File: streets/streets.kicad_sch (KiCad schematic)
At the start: 11 parts, among them J1 Barrel_Jack, J2 Conn_02x20_Odd_Even, J3 Conn_02x20_Odd_Even, J4 Conn_02x20_Odd_Even, J5 Conn_02x20_Odd_Even

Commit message: feat: refactor to use bus
Signed-off-by: Matt Gleich <git@mattglei.ch>
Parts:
- removed S2: M2012SA1W03, M2012SA1W03, symbol M2012SA1W03:M2012SA1W03
- J2: value Conn_02x20_Odd_Even -> Raspberry Pi Zero W 2 (mg01)
- J3: value Conn_02x20_Odd_Even -> Adafruit eINK Bonnet
- J4: value Conn_02x20_Odd_Even -> CharliePlex Bonnet
- J5: value Conn_02x20_Odd_Even -> Blinkt!
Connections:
- net at D1.2 (A), J1.2, J4.6 (Pin_6): now also D2.1 (K), J3.6 (Pin_6), J5.6 (Pin_6); no longer D2.2 (A), J2.6 (Pin_6)
- net at J1.1, S1.2 (COM): no longer R2.1
- net at S1.3 (ON): now also J2.2 (Pin_2), J3.2 (Pin_2), J4.2 (Pin_2), J5.4 (Pin_4), R2.2; no longer J2.4 (Pin_4)
- net at J2.1 (Pin_1), J3.1 (Pin_1): now also J4.1 (Pin_1)
- net at J2.10 (Pin_10): no longer J3.10 (Pin_10)
- net at J2.12 (Pin_12): no longer J3.12 (Pin_12)
- net at J2.14 (Pin_14): no longer J3.14 (Pin_14)
- net at J2.16 (Pin_16): now also J4.16 (Pin_16); no longer J3.16 (Pin_16)
- net at J2.17 (Pin_17): no longer J3.17 (Pin_17)
- net at J2.18 (Pin_18): now also J4.18 (Pin_18); no longer J3.18 (Pin_18)
- net at J2.20 (Pin_20): no longer J3.20 (Pin_20)
- net at J2.21 (Pin_21): no longer J3.21 (Pin_21)
- net at J2.22 (Pin_22): no longer J3.22 (Pin_22)
- net at J2.25 (Pin_25): no longer J3.25 (Pin_25)
- net at J2.26 (Pin_26): no longer J3.26 (Pin_26)
- net at J2.27 (Pin_27): no longer J3.27 (Pin_27)
- net at J2.28 (Pin_28): no longer J3.28 (Pin_28)
- net at J2.3 (Pin_3), J3.3 (Pin_3): now also J5.3 (Pin_3)
- net at J2.30 (Pin_30): no longer J3.30 (Pin_30)
- net at J2.32 (Pin_32): no longer J3.32 (Pin_32)
- net at J2.33 (Pin_33): no longer J3.33 (Pin_33)
- net at J2.34 (Pin_34): no longer J3.34 (Pin_34)
- net at J2.35 (Pin_35): no longer J3.35 (Pin_35)
- net at J2.36 (Pin_36): no longer J3.36 (Pin_36)
- net at J2.37 (Pin_37): no longer J3.37 (Pin_37)
- net at J2.38 (Pin_38): no longer J3.38 (Pin_38)
- net at J2.39 (Pin_39): no longer J3.39 (Pin_39)
- net at J2.40 (Pin_40): no longer J3.40 (Pin_40)
- net at J2.5 (Pin_5), J3.5 (Pin_5): now also J5.5 (Pin_5)
- net at J2.7 (Pin_7): no longer J3.7 (Pin_7)
- net at J2.8 (Pin_8): no longer J3.8 (Pin_8)
- net at J2.9 (Pin_9): no longer J3.9 (Pin_9)
- net at J5.1 (Pin_1): no longer J4.1 (Pin_1)
- net at J4.10 (Pin_10): no longer J5.10 (Pin_10)
- net at J4.11 (Pin_11): no longer J5.11 (Pin_11)
- net at J4.12 (Pin_12): no longer J5.12 (Pin_12)
- net at J4.13 (Pin_13): no longer J5.13 (Pin_13)
- net at J4.14 (Pin_14): no longer J5.14 (Pin_14)
- net at J4.15 (Pin_15): no longer J5.15 (Pin_15)
- net at J5.16 (Pin_16): no longer J4.16 (Pin_16)
- net at J4.17 (Pin_17): no longer J5.17 (Pin_17)
- net at J5.18 (Pin_18): no longer J4.18 (Pin_18)
- net at J4.19 (Pin_19): no longer J5.19 (Pin_19)
- net at J5.2 (Pin_2): no longer J4.2 (Pin_2)
- net at J4.20 (Pin_20): no longer J5.20 (Pin_20)
- net at J4.21 (Pin_21): no longer J5.21 (Pin_21)
- net at J4.22 (Pin_22): no longer J5.22 (Pin_22)
- net at J4.23 (Pin_23): no longer J5.23 (Pin_23)
- net at J4.24 (Pin_24): no longer J5.24 (Pin_24)
- net at J4.25 (Pin_25): no longer J5.25 (Pin_25)
- net at J4.26 (Pin_26): no longer J5.26 (Pin_26)
- net at J4.27 (Pin_27): no longer J5.27 (Pin_27)
- net at J4.28 (Pin_28): no longer J5.28 (Pin_28)
- net at J4.29 (Pin_29): no longer J5.29 (Pin_29)
- net at J4.3 (Pin_3): no longer J5.3 (Pin_3)
- net at J4.30 (Pin_30): no longer J5.30 (Pin_30)
- net at J4.31 (Pin_31): no longer J5.31 (Pin_31)
- net at J4.32 (Pin_32): no longer J5.32 (Pin_32)
- net at J4.33 (Pin_33): no longer J5.33 (Pin_33)
- net at J4.34 (Pin_34): no longer J5.34 (Pin_34)
- net at J4.35 (Pin_35): no longer J5.35 (Pin_35)
- net at J4.36 (Pin_36): no longer J5.36 (Pin_36)
- net at J4.37 (Pin_37): no longer J5.37 (Pin_37)
- net at J4.38 (Pin_38): no longer J5.38 (Pin_38)
- net at J4.39 (Pin_39): no longer J5.39 (Pin_39)
- net at J4.40 (Pin_40): no longer J5.40 (Pin_40)
- net at J4.5 (Pin_5): no longer J5.5 (Pin_5)
- net at J4.7 (Pin_7): no longer J5.7 (Pin_7)
- net at J4.8 (Pin_8): no longer J5.8 (Pin_8)
- net at J4.9 (Pin_9): no longer J5.9 (Pin_9)
- new net: D2.2 (A), R2.1
- no-connect marks 0 -> 124
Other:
- note added: "OFF INDICATOR"
- note added: "ON INDICATOR"
- note added: "mg01 MAIN BUS"

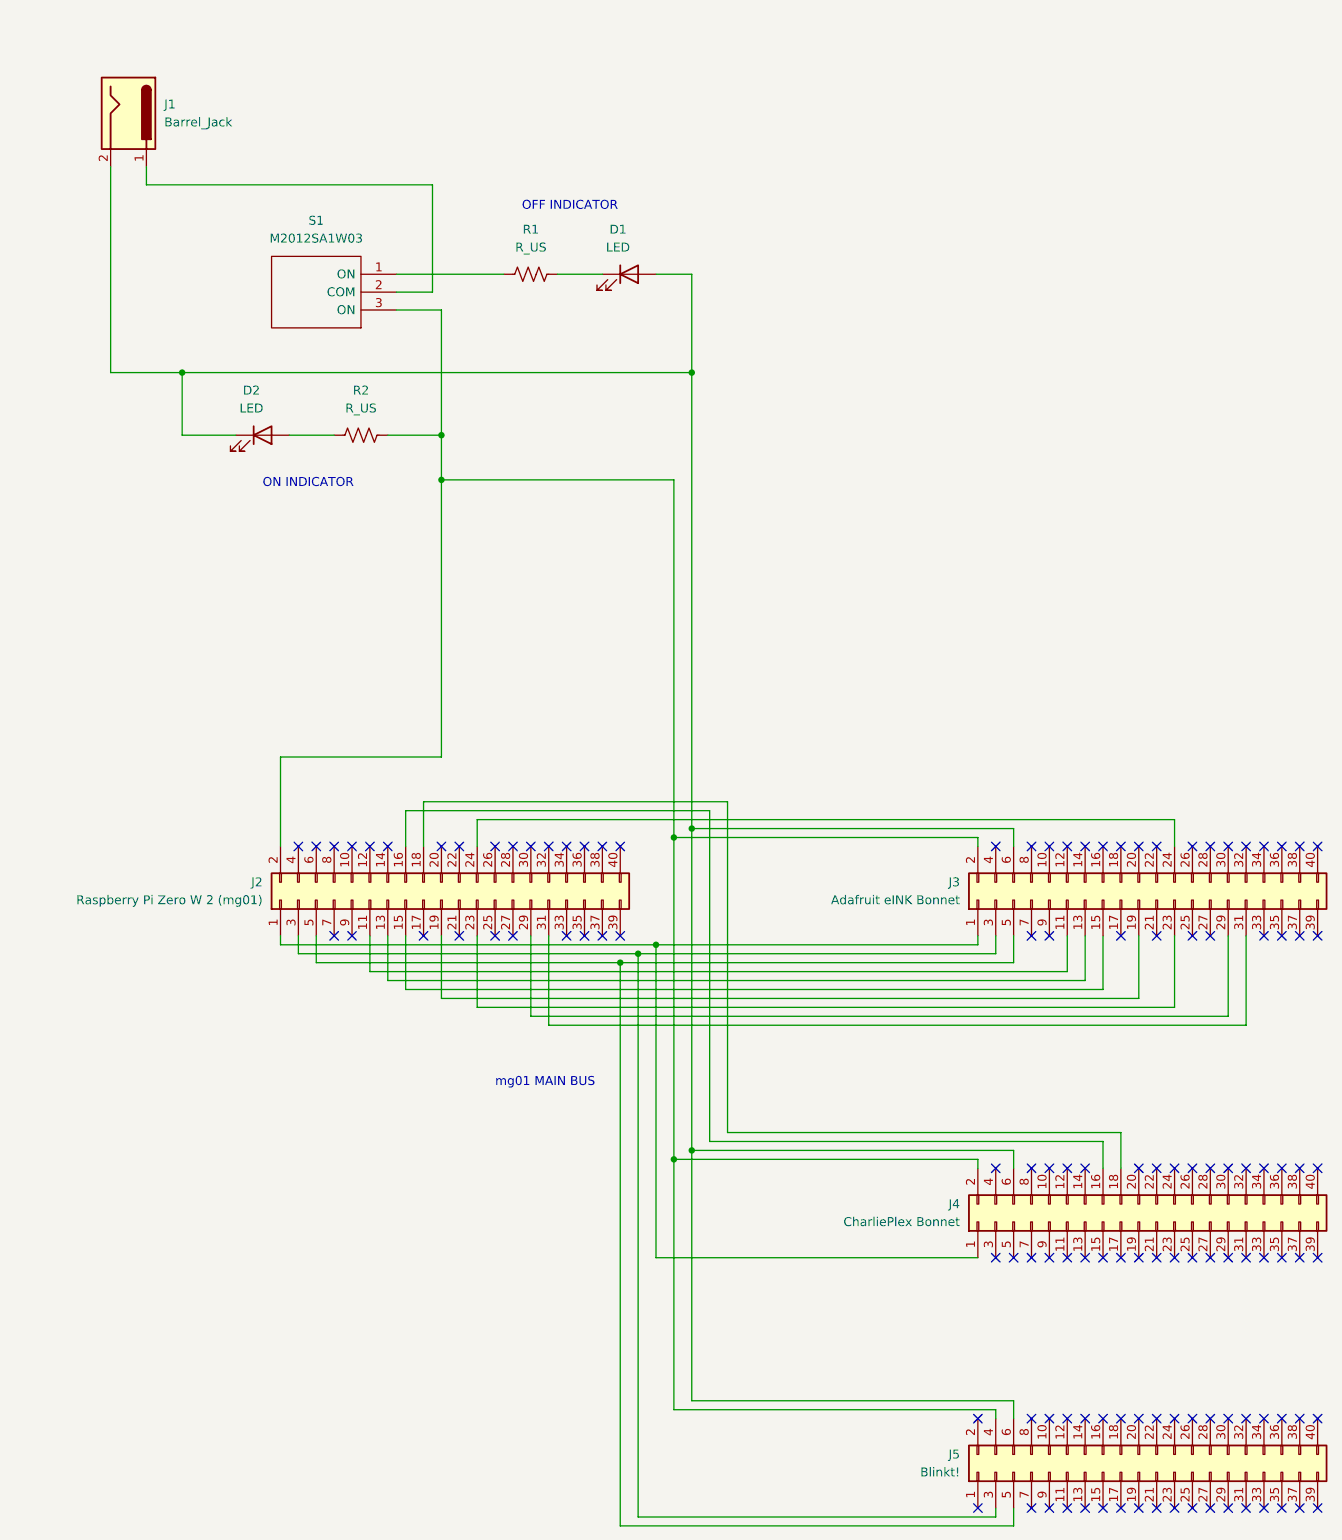
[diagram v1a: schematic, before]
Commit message: feat: setup proper bus from pi
Signed-off-by: Matt Gleich <git@mattglei.ch>
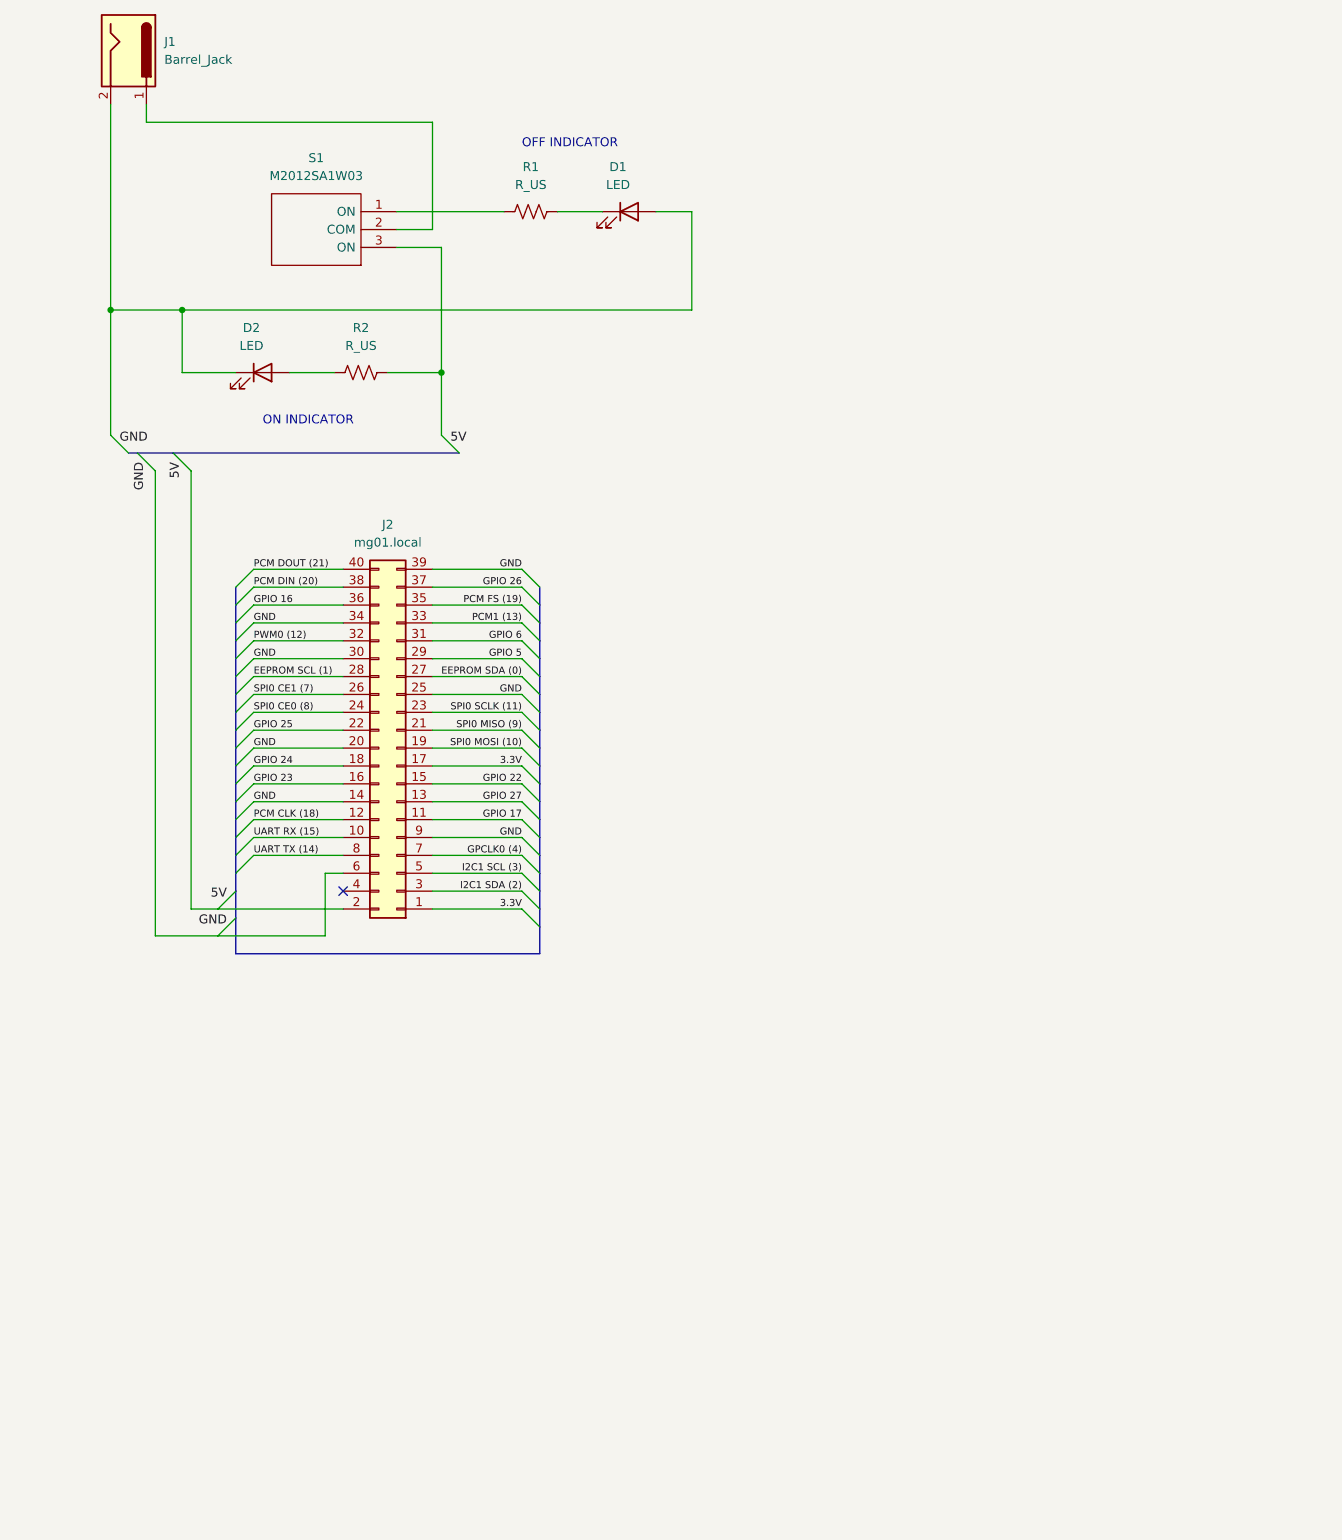
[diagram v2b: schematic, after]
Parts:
- removed J3: Adafruit eINK Bonnet, symbol Connector_Generic:Conn_02x20_Odd_Even
- removed J4: CharliePlex Bonnet, symbol Connector_Generic:Conn_02x20_Odd_Even
- removed J5: Blinkt!, symbol Connector_Generic:Conn_02x20_Odd_Even
- J2: value Raspberry Pi Zero W 2 (mg01) -> mg01.local
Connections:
- net 3.3V: now reaches J2.1 (Pin_1)
- net 3.3V: now also J2.17 (Pin_17)
- net GPIO 23: now reaches J2.16 (Pin_16)
- net GPIO 24: now reaches J2.18 (Pin_18)
- net at R2.2, S1.3 (ON): no longer J2.2 (Pin_2)
- net I2C1 SDA (2): now reaches J2.3 (Pin_3)
- net I2C1 SCL (3): now reaches J2.5 (Pin_5)
- net UART RX (15): now reaches J2.10 (Pin_10)
- net GPIO 17: now reaches J2.11 (Pin_11)
- net PCM CLK (18): now reaches J2.12 (Pin_12)
- net GPIO 27: now reaches J2.13 (Pin_13)
- net GND: now reaches J2.14 (Pin_14)
- net GND: now also J2.20 (Pin_20), J2.25 (Pin_25), J2.30 (Pin_30), J2.34 (Pin_34), J2.39 (Pin_39), J2.9 (Pin_9)
- net GPIO 22: now reaches J2.15 (Pin_15)
- net SPI0 MOSI (10): now reaches J2.19 (Pin_19)
- net SPI0 MISO (9): now reaches J2.21 (Pin_21)
- net GPIO 25: now reaches J2.22 (Pin_22)
- net SPI0 SCLK (11): now reaches J2.23 (Pin_23)
- net SPI0 CE0 (8): now reaches J2.24 (Pin_24)
- net SPI0 CE1 (7): now reaches J2.26 (Pin_26)
- net EEPROM SDA (0): now reaches J2.27 (Pin_27)
- net EEPROM SCL (1): now reaches J2.28 (Pin_28)
- net GPIO 5: now reaches J2.29 (Pin_29)
- net GPIO 6: now reaches J2.31 (Pin_31)
- net PWM0 (12): now reaches J2.32 (Pin_32)
- net PCM1 (13): now reaches J2.33 (Pin_33)
- net PCM FS (19): now reaches J2.35 (Pin_35)
- net GPIO 16: now reaches J2.36 (Pin_36)
- net GPIO 26: now reaches J2.37 (Pin_37)
- net PCM DIN (20): now reaches J2.38 (Pin_38)
- net PCM DOUT (21): now reaches J2.40 (Pin_40)
- net GPCLK0 (4): now reaches J2.7 (Pin_7)
- net UART TX (14): now reaches J2.8 (Pin_8)
- no-connect marks 124 -> 1
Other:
- note removed: "mg01 MAIN BUS"
- moved on the sheet: D1, D2, J1, R1, R2, S1

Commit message: feat: full board
Signed-off-by: Matt Gleich <git@mattglei.ch>
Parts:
- added Brd?: SSD1306, symbol SSD1306:SSD1306
- added D3, D4, D5, D6, D7, D8: LED, symbol Device:LED
- added J10, J?: mg03.local, symbol Connector_Generic:Conn_02x20_Odd_Even
- added J11, J12, J13, J3, J4, J5, J7, J8, J9: Conn_02x20_Odd_Even, symbol Connector_Generic:Conn_02x20_Odd_Even
- added J6: mg02.local, symbol Connector_Generic:Conn_02x20_Odd_Even
- added R3, R4, R5, R6, R7, R8: R_US, symbol Device:R_US
- added S2, S3, S4: M2012SA1W03, M2012SA1W03, symbol M2012SA1W03:M2012SA1W03
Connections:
- net 3.3V: now also J10.1 (Pin_1), J10.17 (Pin_17), J11.1 (Pin_1), J11.17 (Pin_17), J12.1 (Pin_1), J12.17 (Pin_17), J13.1 (Pin_1), J13.17 (Pin_17), J3.1 (Pin_1), J3.17 (Pin_17), J4.1 (Pin_1), J4.17 (Pin_17), J5.1 (Pin_1), J5.17 (Pin_17), J6.1 (Pin_1), J6.17 (Pin_17), J7.1 (Pin_1), J7.17 (Pin_17), J8.1 (Pin_1), J8.17 (Pin_17), J9.1 (Pin_1), J9.17 (Pin_17)
- net 5V: now also J2.2 (Pin_2), R2.2, S1.3 (ON), J10.2 (Pin_2), J11.2 (Pin_2), J11.4 (Pin_4), J12.2 (Pin_2), J12.4 (Pin_4), J13.2 (Pin_2), J13.4 (Pin_4), J3.2 (Pin_2), J3.4 (Pin_4), J4.2 (Pin_2), J4.4 (Pin_4), J5.2 (Pin_2), J5.4 (Pin_4), J6.2 (Pin_2), J7.2 (Pin_2), J7.4 (Pin_4), J8.2 (Pin_2), J8.4 (Pin_4), J9.2 (Pin_2), J9.4 (Pin_4), J?.4 (Pin_4), R3.2, R5.2, R7.2, S2.3 (ON), S3.3 (ON), S4.3 (ON)
- net EEPROM SCL (1): now also J10.28 (Pin_28), J11.28 (Pin_28), J12.28 (Pin_28), J13.28 (Pin_28), J3.28 (Pin_28), J4.28 (Pin_28), J5.28 (Pin_28), J6.28 (Pin_28), J7.28 (Pin_28), J8.28 (Pin_28), J9.28 (Pin_28)
- net EEPROM SDA (0): now also J10.27 (Pin_27), J11.27 (Pin_27), J12.27 (Pin_27), J13.27 (Pin_27), J3.27 (Pin_27), J4.27 (Pin_27), J5.27 (Pin_27), J6.27 (Pin_27), J7.27 (Pin_27), J8.27 (Pin_27), J9.27 (Pin_27)
- net GND: now also D1.2 (A), D2.1 (K), J1.2, J2.6 (Pin_6), D3.1 (K), D4.2 (A), D5.1 (K), D6.2 (A), D7.1 (K), D8.2 (A), J10.14 (Pin_14), J10.20 (Pin_20), J10.25 (Pin_25), J10.30 (Pin_30), J10.34 (Pin_34), J10.39 (Pin_39), J10.6 (Pin_6), J10.9 (Pin_9), J11.14 (Pin_14), J11.20 (Pin_20), J11.25 (Pin_25), J11.30 (Pin_30), J11.34 (Pin_34), J11.39 (Pin_39), J11.6 (Pin_6), J11.9 (Pin_9), J12.14 (Pin_14), J12.20 (Pin_20), J12.25 (Pin_25), J12.30 (Pin_30), J12.34 (Pin_34), J12.39 (Pin_39), J12.6 (Pin_6), J12.9 (Pin_9), J13.14 (Pin_14), J13.20 (Pin_20), J13.25 (Pin_25), J13.30 (Pin_30), J13.34 (Pin_34), J13.39 (Pin_39), J13.6 (Pin_6), J13.9 (Pin_9), J3.14 (Pin_14), J3.20 (Pin_20), J3.25 (Pin_25), J3.30 (Pin_30), J3.34 (Pin_34), J3.39 (Pin_39), J3.6 (Pin_6), J3.9 (Pin_9), J4.14 (Pin_14), J4.20 (Pin_20), J4.25 (Pin_25), J4.30 (Pin_30), J4.34 (Pin_34), J4.39 (Pin_39), J4.6 (Pin_6), J4.9 (Pin_9), J5.14 (Pin_14), J5.20 (Pin_20), J5.25 (Pin_25), J5.30 (Pin_30), J5.34 (Pin_34), J5.39 (Pin_39), J5.6 (Pin_6), J5.9 (Pin_9), J6.14 (Pin_14), J6.20 (Pin_20), J6.25 (Pin_25), J6.30 (Pin_30), J6.34 (Pin_34), J6.39 (Pin_39), J6.6 (Pin_6), J6.9 (Pin_9), J7.14 (Pin_14), J7.20 (Pin_20), J7.25 (Pin_25), J7.30 (Pin_30), J7.34 (Pin_34), J7.39 (Pin_39), J7.6 (Pin_6), J7.9 (Pin_9), J8.14 (Pin_14), J8.20 (Pin_20), J8.25 (Pin_25), J8.30 (Pin_30), J8.34 (Pin_34), J8.39 (Pin_39), J8.6 (Pin_6), J8.9 (Pin_9), J9.14 (Pin_14), J9.20 (Pin_20), J9.25 (Pin_25), J9.30 (Pin_30), J9.34 (Pin_34), J9.39 (Pin_39), J9.6 (Pin_6), J9.9 (Pin_9), J?.6 (Pin_6)
- net GPCLK0 (4): now also J10.7 (Pin_7), J11.7 (Pin_7), J12.7 (Pin_7), J13.7 (Pin_7), J3.7 (Pin_7), J4.7 (Pin_7), J5.7 (Pin_7), J6.7 (Pin_7), J7.7 (Pin_7), J8.7 (Pin_7), J9.7 (Pin_7)
- net GPIO 16: now also J10.36 (Pin_36), J11.36 (Pin_36), J12.36 (Pin_36), J13.36 (Pin_36), J3.36 (Pin_36), J4.36 (Pin_36), J5.36 (Pin_36), J6.36 (Pin_36), J7.36 (Pin_36), J8.36 (Pin_36), J9.36 (Pin_36)
- net GPIO 17: now also J10.11 (Pin_11), J11.11 (Pin_11), J12.11 (Pin_11), J13.11 (Pin_11), J3.11 (Pin_11), J4.11 (Pin_11), J5.11 (Pin_11), J6.11 (Pin_11), J7.11 (Pin_11), J8.11 (Pin_11), J9.11 (Pin_11)
- net GPIO 22: now also J10.15 (Pin_15), J11.15 (Pin_15), J12.15 (Pin_15), J13.15 (Pin_15), J3.15 (Pin_15), J4.15 (Pin_15), J5.15 (Pin_15), J6.15 (Pin_15), J7.15 (Pin_15), J8.15 (Pin_15), J9.15 (Pin_15)
- net GPIO 23: now also J10.16 (Pin_16), J11.16 (Pin_16), J12.16 (Pin_16), J13.16 (Pin_16), J3.16 (Pin_16), J4.16 (Pin_16), J5.16 (Pin_16), J6.16 (Pin_16), J7.16 (Pin_16), J8.16 (Pin_16), J9.16 (Pin_16)
- net GPIO 24: now also J10.18 (Pin_18), J11.18 (Pin_18), J12.18 (Pin_18), J13.18 (Pin_18), J3.18 (Pin_18), J4.18 (Pin_18), J5.18 (Pin_18), J6.18 (Pin_18), J7.18 (Pin_18), J8.18 (Pin_18), J9.18 (Pin_18)
- net GPIO 25: now also J10.22 (Pin_22), J11.22 (Pin_22), J12.22 (Pin_22), J13.22 (Pin_22), J3.22 (Pin_22), J4.22 (Pin_22), J5.22 (Pin_22), J6.22 (Pin_22), J7.22 (Pin_22), J8.22 (Pin_22), J9.22 (Pin_22)
- net GPIO 26: now also J10.37 (Pin_37), J11.37 (Pin_37), J12.37 (Pin_37), J13.37 (Pin_37), J3.37 (Pin_37), J4.37 (Pin_37), J5.37 (Pin_37), J6.37 (Pin_37), J7.37 (Pin_37), J8.37 (Pin_37), J9.37 (Pin_37)
- net GPIO 27: now also J10.13 (Pin_13), J11.13 (Pin_13), J12.13 (Pin_13), J13.13 (Pin_13), J3.13 (Pin_13), J4.13 (Pin_13), J5.13 (Pin_13), J6.13 (Pin_13), J7.13 (Pin_13), J8.13 (Pin_13), J9.13 (Pin_13)
- net GPIO 5: now also J10.29 (Pin_29), J11.29 (Pin_29), J12.29 (Pin_29), J13.29 (Pin_29), J3.29 (Pin_29), J4.29 (Pin_29), J5.29 (Pin_29), J6.29 (Pin_29), J7.29 (Pin_29), J8.29 (Pin_29), J9.29 (Pin_29)
- net GPIO 6: now also J10.31 (Pin_31), J11.31 (Pin_31), J12.31 (Pin_31), J13.31 (Pin_31), J3.31 (Pin_31), J4.31 (Pin_31), J5.31 (Pin_31), J6.31 (Pin_31), J7.31 (Pin_31), J8.31 (Pin_31), J9.31 (Pin_31)
- net I2C1 SCL (3): now also J10.5 (Pin_5), J11.5 (Pin_5), J12.5 (Pin_5), J13.5 (Pin_5), J3.5 (Pin_5), J4.5 (Pin_5), J5.5 (Pin_5), J6.5 (Pin_5), J7.5 (Pin_5), J8.5 (Pin_5), J9.5 (Pin_5)
- net I2C1 SDA (2): now also J10.3 (Pin_3), J11.3 (Pin_3), J12.3 (Pin_3), J13.3 (Pin_3), J3.3 (Pin_3), J4.3 (Pin_3), J5.3 (Pin_3), J6.3 (Pin_3), J7.3 (Pin_3), J8.3 (Pin_3), J9.3 (Pin_3)
- net PCM CLK (18): now also J10.12 (Pin_12), J11.12 (Pin_12), J12.12 (Pin_12), J13.12 (Pin_12), J3.12 (Pin_12), J4.12 (Pin_12), J5.12 (Pin_12), J6.12 (Pin_12), J7.12 (Pin_12), J8.12 (Pin_12), J9.12 (Pin_12)
- net PCM DIN (20): now also J10.38 (Pin_38), J11.38 (Pin_38), J12.38 (Pin_38), J13.38 (Pin_38), J3.38 (Pin_38), J4.38 (Pin_38), J5.38 (Pin_38), J6.38 (Pin_38), J7.38 (Pin_38), J8.38 (Pin_38), J9.38 (Pin_38)
- net PCM DOUT (21): now also J10.40 (Pin_40), J11.40 (Pin_40), J12.40 (Pin_40), J13.40 (Pin_40), J3.40 (Pin_40), J4.40 (Pin_40), J5.40 (Pin_40), J6.40 (Pin_40), J7.40 (Pin_40), J8.40 (Pin_40), J9.40 (Pin_40)
- net PCM FS (19): now also J10.35 (Pin_35), J11.35 (Pin_35), J12.35 (Pin_35), J13.35 (Pin_35), J3.35 (Pin_35), J4.35 (Pin_35), J5.35 (Pin_35), J6.35 (Pin_35), J7.35 (Pin_35), J8.35 (Pin_35), J9.35 (Pin_35)
- net PCM1 (13): now also J10.33 (Pin_33), J11.33 (Pin_33), J12.33 (Pin_33), J13.33 (Pin_33), J3.33 (Pin_33), J4.33 (Pin_33), J5.33 (Pin_33), J6.33 (Pin_33), J7.33 (Pin_33), J8.33 (Pin_33), J9.33 (Pin_33)
- net PWM0 (12): now also J10.32 (Pin_32), J11.32 (Pin_32), J12.32 (Pin_32), J13.32 (Pin_32), J3.32 (Pin_32), J4.32 (Pin_32), J5.32 (Pin_32), J6.32 (Pin_32), J7.32 (Pin_32), J8.32 (Pin_32), J9.32 (Pin_32)
- net SPI0 CE0 (8): now also J10.24 (Pin_24), J11.24 (Pin_24), J12.24 (Pin_24), J13.24 (Pin_24), J3.24 (Pin_24), J4.24 (Pin_24), J5.24 (Pin_24), J6.24 (Pin_24), J7.24 (Pin_24), J8.24 (Pin_24), J9.24 (Pin_24)
- net SPI0 CE1 (7): now also J10.26 (Pin_26), J11.26 (Pin_26), J12.26 (Pin_26), J13.26 (Pin_26), J3.26 (Pin_26), J4.26 (Pin_26), J5.26 (Pin_26), J6.26 (Pin_26), J7.26 (Pin_26), J8.26 (Pin_26), J9.26 (Pin_26)
- net SPI0 MISO (9): now also J10.21 (Pin_21), J11.21 (Pin_21), J12.21 (Pin_21), J13.21 (Pin_21), J3.21 (Pin_21), J4.21 (Pin_21), J5.21 (Pin_21), J6.21 (Pin_21), J7.21 (Pin_21), J8.21 (Pin_21), J9.21 (Pin_21)
- net SPI0 MOSI (10): now also J10.19 (Pin_19), J11.19 (Pin_19), J12.19 (Pin_19), J13.19 (Pin_19), J3.19 (Pin_19), J4.19 (Pin_19), J5.19 (Pin_19), J6.19 (Pin_19), J7.19 (Pin_19), J8.19 (Pin_19), J9.19 (Pin_19)
- net SPI0 SCLK (11): now also J10.23 (Pin_23), J11.23 (Pin_23), J12.23 (Pin_23), J13.23 (Pin_23), J3.23 (Pin_23), J4.23 (Pin_23), J5.23 (Pin_23), J6.23 (Pin_23), J7.23 (Pin_23), J8.23 (Pin_23), J9.23 (Pin_23)
- net UART RX (15): now also J10.10 (Pin_10), J11.10 (Pin_10), J12.10 (Pin_10), J13.10 (Pin_10), J3.10 (Pin_10), J4.10 (Pin_10), J5.10 (Pin_10), J6.10 (Pin_10), J7.10 (Pin_10), J8.10 (Pin_10), J9.10 (Pin_10)
- net UART TX (14): now also J10.8 (Pin_8), J11.8 (Pin_8), J12.8 (Pin_8), J13.8 (Pin_8), J3.8 (Pin_8), J4.8 (Pin_8), J5.8 (Pin_8), J6.8 (Pin_8), J7.8 (Pin_8), J8.8 (Pin_8), J9.8 (Pin_8)
- net at J1.1, S1.2 (COM): now also S2.2 (COM), S3.2 (COM), S4.2 (COM)
- new net: R8.1, S4.1 (ON)
- new net: D7.2 (A), R7.1
- new net: R6.1, S3.1 (ON)
- new net: Brd?.1 (GND), J?.9 (Pin_9)
- new net: Brd?.2 (VCC), J?.2 (Pin_2)
- new net: Brd?.3 (SCL), J?.3 (Pin_3)
- new net: Brd?.4 (SDA), J?.5 (Pin_5)
- new net: R4.1, S2.1 (ON)
- new net: D3.2 (A), R3.1
- new net: D8.1 (K), R8.2
- new net: D6.1 (K), R6.2
- new net: D4.1 (K), R4.2
- new net: D5.2 (A), R5.1
- no-connect marks 1 -> 38
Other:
- note added: "mg01.local"
- note added: "mg02.local"
- note added: "mg03.local"
- moved on the sheet: J2

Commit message: feat: init viper
Signed-off-by: Matt Gleich <git@mattglei.ch>
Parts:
- removed Brd?: SSD1306, symbol SSD1306:SSD1306
- removed D5, D6, D7, D8: LED, symbol Device:LED
- removed J10, J?: mg03.local, symbol Connector_Generic:Conn_02x20_Odd_Even
- removed J11, J12, J13: Conn_02x20_Odd_Even, symbol Connector_Generic:Conn_02x20_Odd_Even
- removed R5, R6, R7, R8: R_US, symbol Device:R_US
- removed S3, S4: M2012SA1W03, M2012SA1W03, symbol M2012SA1W03:M2012SA1W03
- added Brd? (x2): SSD1306, symbol SSD1306:SSD1306
- added D? (x6): LED, symbol Device:LED
- added J? (x3): pico board, symbol Connector_Generic:Conn_02x20_Odd_Even
- added R? (x6): R_US, symbol Device:R_US
- added S? (x3): M2012SA1W03, M2012SA1W03, symbol M2012SA1W03:M2012SA1W03
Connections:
- net 5V: now also J?.4 (Pin_4), J?.4 (Pin_4), J?.4 (Pin_4), R?.2, R?.2, R?.2, S?.3 (ON), S?.3 (ON), S?.3 (ON)
- net GND: now also D?.1 (K), D?.1 (K), D?.1 (K), D?.2 (A), D?.2 (A), D?.2 (A), J?.6 (Pin_6), J?.6 (Pin_6), J?.6 (Pin_6)
- net at J1.1, S1.2 (COM), S2.2 (COM): now also S?.2 (COM), S?.2 (COM)
- new net: D?.2 (A), R?.1 (x3)
- new net: R?.1, S?.1 (ON) (x3)
- new net: D?.1 (K), R?.2 (x3)
- new net: Brd?.2 (VCC), J?.2 (Pin_2) (x2)
- new net: Brd?.3 (SCL), J?.3 (Pin_3) (x2)
- new net: Brd?.4 (SDA), J?.5 (Pin_5) (x2)
- new net: Brd?.1 (GND), J?.9 (Pin_9) (x2)
- no-connect marks 38 -> 107
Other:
- note added: "mark 1"
- note added: "mark 2"
- note removed: "mg01.local"
- note removed: "mg02.local"
- note removed: "mg03.local"

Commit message: feat: setup viper sch
Signed-off-by: Matt Gleich <git@mattglei.ch>
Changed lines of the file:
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@@
-    (stroke (width 0) (type default) (color 0 0 0 0))
-  )
-  (wire (pts (xy 323.85 116.84) (xy 351.79 116.84))
     (stroke (width 0) (type default) (color 0 0 0 0))
   )
